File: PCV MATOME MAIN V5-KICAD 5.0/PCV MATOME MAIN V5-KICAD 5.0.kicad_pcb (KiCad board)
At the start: 2 copper layers, 195.1 x 113 mm, 88 parts, among them J1 Conn_02x08_Odd_Even, J10 Conn_01x08, J11 Conn_01x02, J12 Conn_01x02, J2 Conn_02x08_Odd_Even, J3 Conn_01x06, J4 Conn_01x06, J5 Conn_01x08, J6 Conn_01x08, J7 Conn_01x02, J8 Conn_01x16, J9 Conn_01x04, P1 Power, P10 CONN_01X01, P11 CONN_01X01, P12 CONN_01X01, P13 CONN_01X01, P2 Analog, P3 Analog, P4 Digital, P5 PWM, P6 PWM, P7 Communication, P8 CONN_01X01, P9 CONN_01X01, Q1 BSS138, Q2 BSS138, Q3 2SC1815, SW1 SW_Push, U1 MAX7219, U2 ESP-12F, U3 MAX7219, U4 SHIFT_LEVEL_3.3V_5V, U5 LM1117-3.3, U6 LD1117S50TR_SOT223

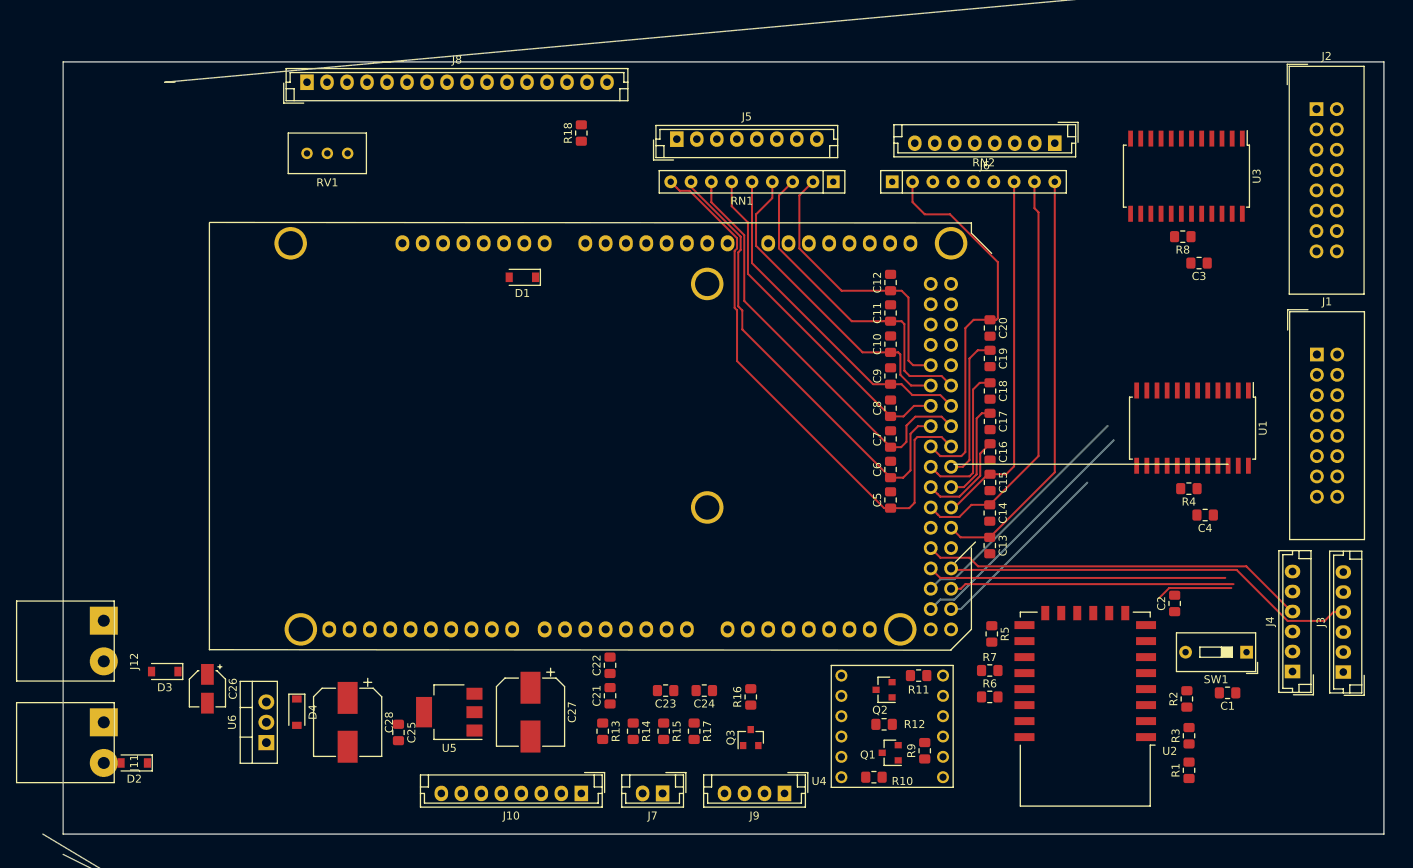
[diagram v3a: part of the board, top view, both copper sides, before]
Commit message: wiring pcb outline
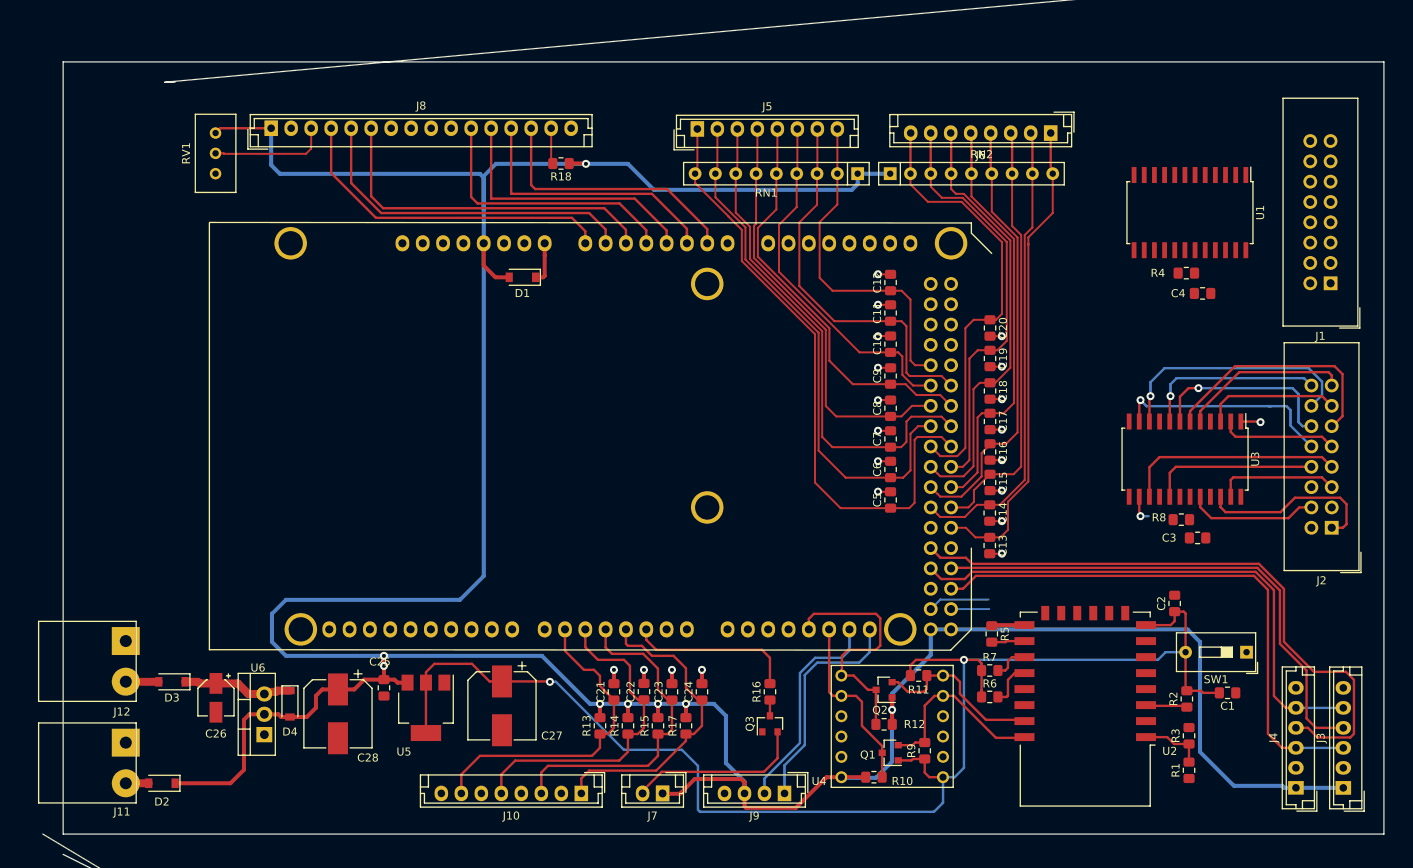
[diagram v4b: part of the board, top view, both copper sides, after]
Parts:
- moved J2 52.4 mm to (247.5, 106.5), turned to 180 degrees
- moved R8 35.4 mm to (228.7, 105.5)
- moved U3 35.4 mm to (229.1, 97.9)
- moved C3 34.4 mm to (230.7, 107.8)
- moved C4 27.7 mm to (231.3, 77.2)
- moved R4 26.9 mm to (229.3, 74.7)
- moved U1 26.9 mm to (229.8, 67.1)
- moved J4 14.5 mm to (243.0, 139.0)
- moved J3 14.5 mm to (248.9, 139.0)
- moved RV1 11.7 mm to (108.0, 57.1), turned to 90 degrees
- moved J1 9.07 mm to (247.3, 75.9), turned to 180 degrees
- moved J8 7.29 mm to (114.9, 56.5)
- moved C25 5.87 mm to (129.0, 126.5)
- moved C22 5.37 mm to (161.5, 127.0)
- moved R18 4.58 mm to (151.1, 61.0), turned to 180 degrees
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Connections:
- J8 pad 3: GND -> Net-(J8-Pad3)
- RV1 pad 2: GND -> Net-(J8-Pad3)
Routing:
- net HV: track 0.00 -> 438.3 mm, vias 0 -> 8
- net LV: track 0.00 -> 174.7 mm, vias 0 -> 2
- net EN: track 0.00 -> 43.8 mm
- net SW4: track 12.3 -> 55.3 mm
- net RW: track 0.00 -> 42.8 mm
- net HOME: track 0.00 -> 42.1 mm
- net RS: track 0.00 -> 41.9 mm
- net BACK: track 0.00 -> 41.3 mm
- net SET: track 0.00 -> 40.5 mm
- net CLK_M: track 40.1 -> 0.00 mm
- net SW5: track 12.8 -> 52.2 mm
- net NEXT: track 0.00 -> 39.1 mm
- net SW6: track 18.8 -> 54.7 mm
- net GND: track 0.00 -> 35.6 mm, vias 0 -> 20
- net D6: track 0.00 -> 35.1 mm
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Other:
- net class 12v added: clearance 0.5, trace_width 1, via_dia 1, via_drill 0.5
- net class 5V added: clearance 0.5, trace_width 0.5, via_dia 1, via_drill 0.5
- net class Default: via_dia 0.6 -> 1; via_drill 0.4 -> 0.5
- net class SIG added: clearance 0.2, trace_width 0.3, via_dia 1, via_drill 0.5

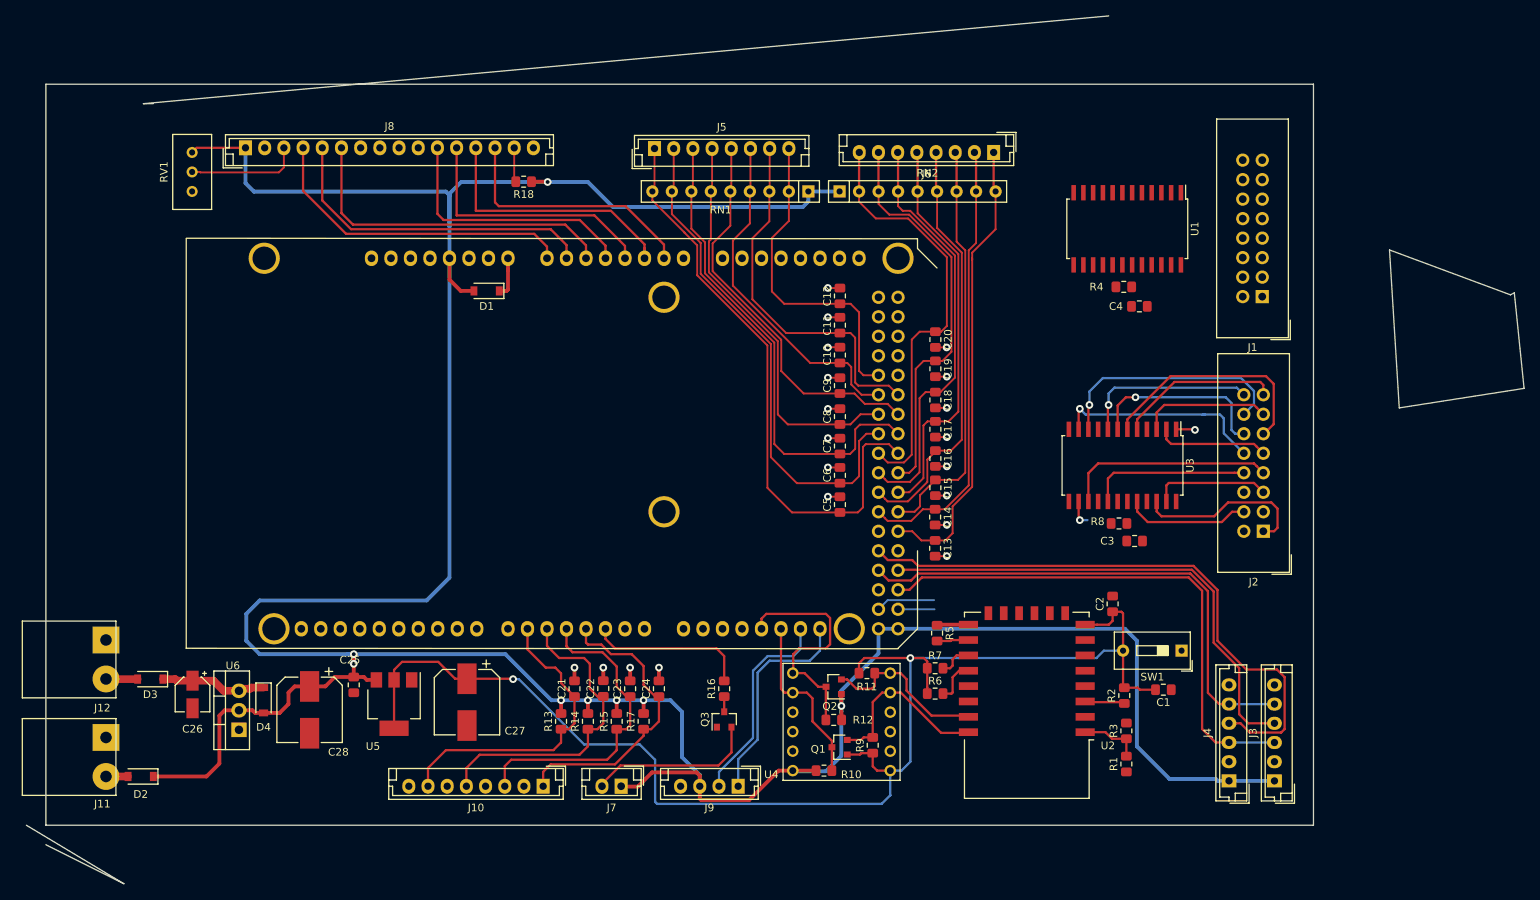
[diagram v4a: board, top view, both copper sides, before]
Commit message: modified pcb 18/08/2018, test pcb final befor release
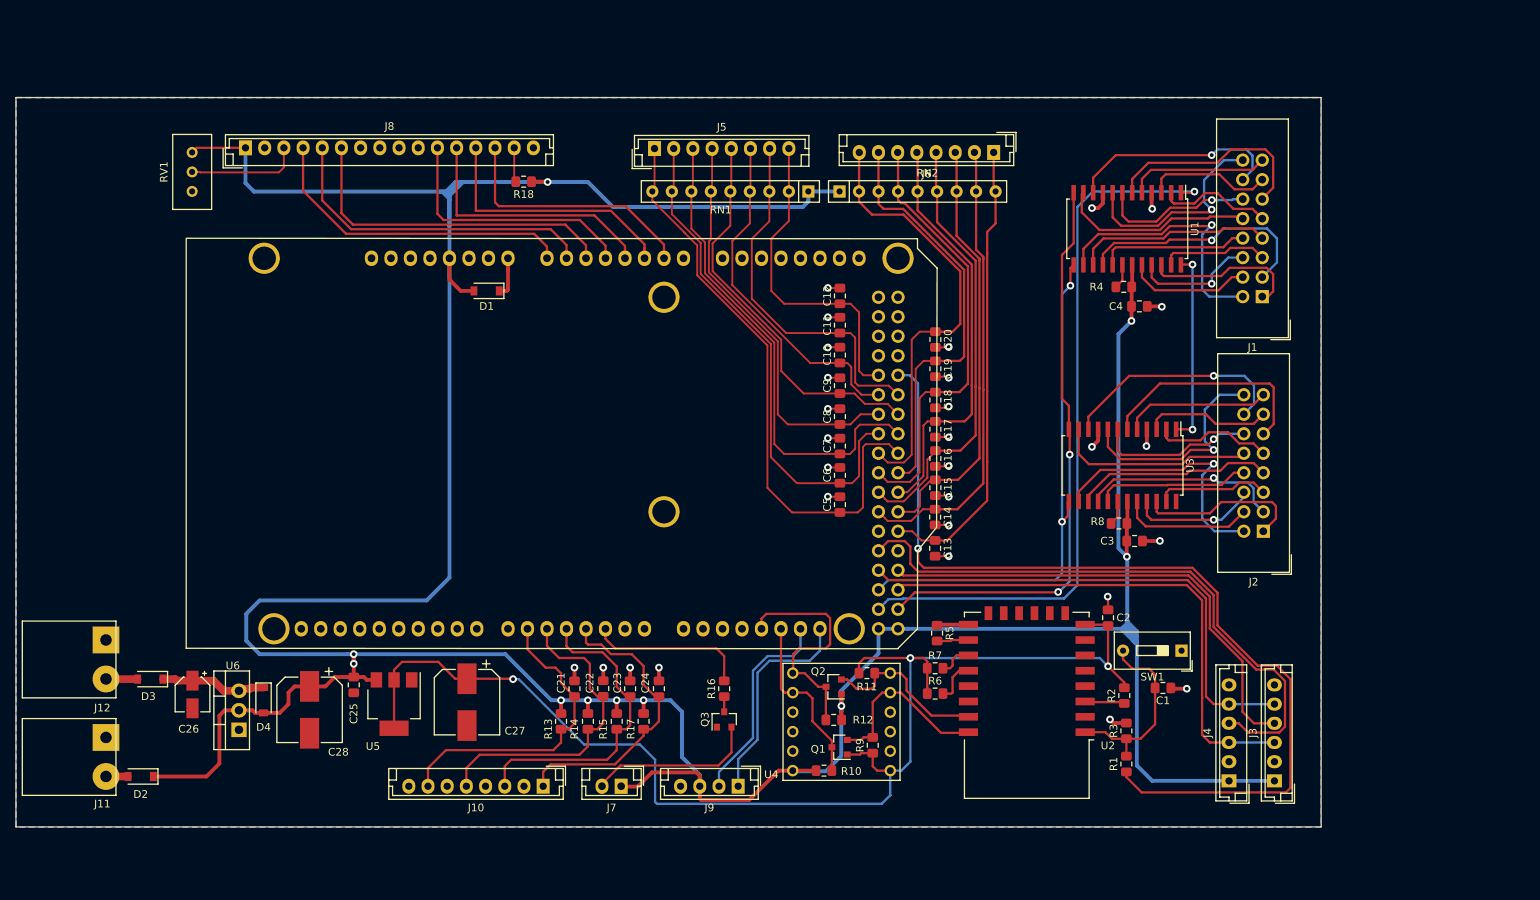
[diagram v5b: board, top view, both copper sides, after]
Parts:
- moved C2 1.89 mm to (227.2, 117.8)
- moved C1 0.23 mm to (234.4, 126.9)
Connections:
- C1 pad 1: GND -> Net-(C1-Pad1)
- C1 pad 2: LV -> Net-(C1-Pad2)
- C10 pad 2: GND -> Net-(C1-Pad1)
- C11 pad 2: GND -> Net-(C1-Pad1)
- C12 pad 2: GND -> Net-(C1-Pad1)
- C13 pad 2: GND -> Net-(C1-Pad1)
- C14 pad 2: GND -> Net-(C1-Pad1)
- C15 pad 2: GND -> Net-(C1-Pad1)
- C16 pad 2: GND -> Net-(C1-Pad1)
- C17 pad 2: GND -> Net-(C1-Pad1)
- C18 pad 2: GND -> Net-(C1-Pad1)
- C19 pad 2: GND -> Net-(C1-Pad1)
- C2 pad 2: GND -> Net-(C1-Pad1)
- C20 pad 2: GND -> Net-(C1-Pad1)
- C21 pad 2: GND -> Net-(C1-Pad1)
- C22 pad 2: GND -> Net-(C1-Pad1)
- C23 pad 2: GND -> Net-(C1-Pad1)
- C24 pad 2: GND -> Net-(C1-Pad1)
- C25 pad 2: GND -> Net-(C1-Pad1)
- C26 pad 2: GND -> Net-(C1-Pad1)
- C27 pad 2: GND -> Net-(C1-Pad1)
- C28 pad 2: GND -> Net-(C1-Pad1)
- C3 pad 1: GND -> Net-(C1-Pad1)
- C4 pad 1: GND -> Net-(C1-Pad1)
- C5 pad 2: GND -> Net-(C1-Pad1)
- C6 pad 2: GND -> Net-(C1-Pad1)
- C7 pad 2: GND -> Net-(C1-Pad1)
- C8 pad 2: GND -> Net-(C1-Pad1)
- C9 pad 2: GND -> Net-(C1-Pad1)
- J10 pad 2: GND -> Net-(C1-Pad1)
- J10 pad 4: GND -> Net-(C1-Pad1)
- J10 pad 6: GND -> Net-(C1-Pad1)
- J10 pad 8: GND -> Net-(C1-Pad1)
- J11 pad 1: GND -> Net-(C1-Pad1)
- J12 pad 1: GND -> Net-(C1-Pad1)
- J3 pad 2: GND -> Net-(C1-Pad1)
- J4 pad 2: GND -> Net-(C1-Pad1)
- J8 pad 16: GND -> (no net)
- J8 pad 2: GND -> Net-(C1-Pad1)
- J9 pad 4: GND -> Net-(C1-Pad1)
- P1 pad 4: LV -> (no net)
- P1 pad 6: GND -> Net-(C1-Pad1)
- P1 pad 7: GND -> Net-(C1-Pad1)
- P4 pad 1: GND -> Net-(C1-Pad1)
- P4 pad 2: GND -> Net-(C1-Pad1)
- P5 pad 1: SCL -> (no net)
- P5 pad 2: SDA -> (no net)
- P5 pad 4: GND -> Net-(C1-Pad1)
- Q3 pad 1: GND -> Net-(C1-Pad1)
- R1 pad 2: Net-(R1-Pad2) -> Net-(C1-Pad2)
- R3 pad 1: Net-(R1-Pad2) -> Net-(C1-Pad2)
- R3 pad 2: GND -> Net-(C1-Pad1)
- R5 pad 1: GND -> Net-(C1-Pad1)
- RV1 pad 3: GND -> Net-(C1-Pad1)
- SW1 pad 1: GND -> Net-(C1-Pad1)
- SW1 pad 2: LV -> Net-(C1-Pad2)
- U1 pad 4: GND -> Net-(C1-Pad1)
- U1 pad 9: GND -> Net-(C1-Pad1)
- U2 pad 1: Net-(R1-Pad2) -> Net-(C1-Pad2)
- U2 pad 15: GND -> Net-(C1-Pad1)
- U3 pad 4: GND -> Net-(C1-Pad1)
- U3 pad 9: GND -> Net-(C1-Pad1)
- U4 pad 11: GND -> Net-(C1-Pad1)
- U4 pad 2: GND -> Net-(C1-Pad1)
- U5 pad 1: GND -> Net-(C1-Pad1)
- U6 pad 1: GND -> Net-(C1-Pad1)
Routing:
- net RESET_ESP: track 0.00 -> 120.9 mm, vias 0 -> 1
- net DIN_M: track 7.72 -> 94.4 mm, vias 0 -> 1
- net HV: track 438.3 -> 514.8 mm, vias 8 -> 10
- net SC_M: track 4.77 -> 75.5 mm, vias 0 -> 2
- net CLK_M: track 0.00 -> 68.6 mm, vias 0 -> 2
- net Net-(C1-Pad1): track 0.00 -> 58.5 mm, vias 0 -> 29
- net GND: track 35.6 -> 0.00 mm, vias 20 -> 0
- net 1-C2: track 0.00 -> 34.7 mm, vias 0 -> 1
- net 1-C3: track 0.00 -> 31.9 mm, vias 0 -> 1
- net 2-C2: track 3.49 -> 34.2 mm
- net 1-R6: track 0.00 -> 28.2 mm, vias 0 -> 1
- net 1-R3: track 0.00 -> 28.2 mm
- net 1-R8: track 0.00 -> 27.8 mm, vias 0 -> 1
- net 1-R2: track 0.00 -> 26.3 mm
- net 2-C3: track 0.00 -> 26.2 mm, vias 0 -> 1
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- added copper zone on B.Cu, net Net-(C1-Pad1)
- added copper zone on F.Cu, net Net-(C1-Pad1)
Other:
- board size 195.1 x 113 mm -> 170 x 95 mm
- net class Default: clearance 0.2 -> 0.25
- rule trace_clearance: 0.2 -> 0.25

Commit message: testing gerber first, add teardrop
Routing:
- net HV: track 514.8 -> 482.6 mm
- net Net-(C1-Pad1): track 58.5 -> 60.4 mm, vias 29 -> 30
- net LV: track 164.8 -> 164.0 mm
- net D6: track 35.1 -> 34.5 mm
- net D5: track 34.0 -> 33.3 mm
